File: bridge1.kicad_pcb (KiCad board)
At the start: 2 copper layers, 64 x 50 mm, 14 parts, among them J1 Conn_01x04, U1 pico

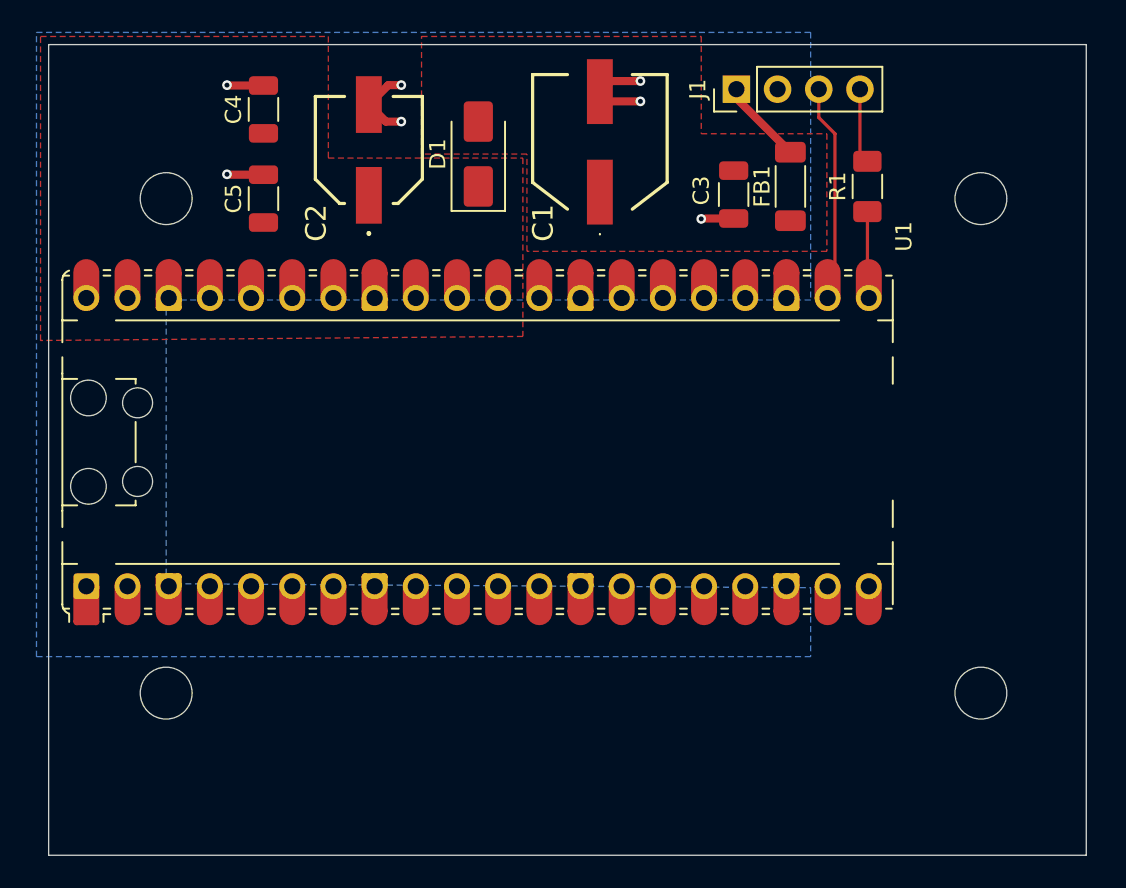
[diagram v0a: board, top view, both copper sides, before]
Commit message: Updated schematic and PCB files to change R1 to 0603 package, J1 to green screw terminal block.
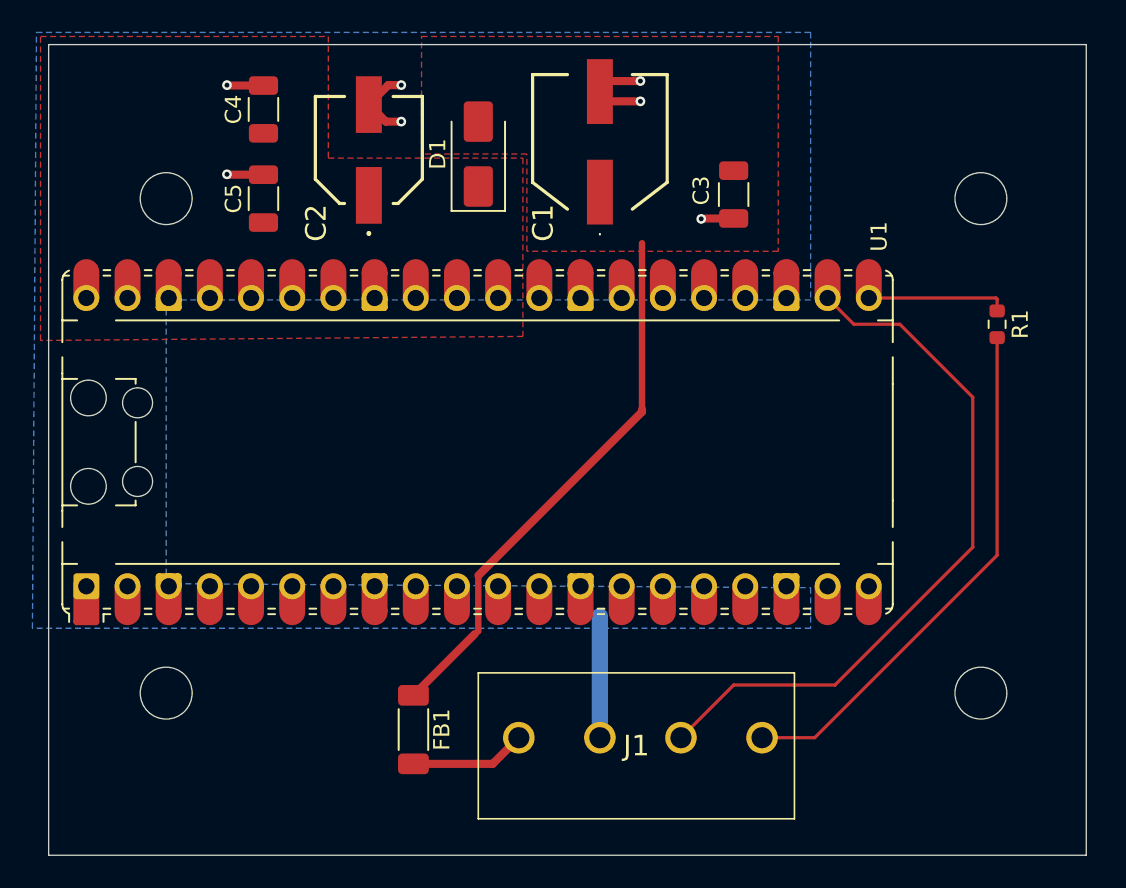
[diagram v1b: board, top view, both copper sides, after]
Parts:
- J1: value Conn_01x04 -> 1935187; footprint Connector_PinHeader_2.54mm:PinHeader_1x04_P2.54mm_Vertical -> Wayne:1935187
- R1: footprint Resistor_SMD:R_1206_3216Metric_Pad1.30x1.75mm_HandSolder -> Resistor_SMD:R_0603_1608Metric
- U1: footprint Wayne:RaspberryPi_Pico_Common_Unspecified -> Module:RaspberryPi_Pico_Common_Unspecified
- moved J1 42.2 mm to (205.0, 88.5), turned to 0 degrees
- moved FB1 40.8 mm to (198.5, 88.0), turned to -90 degrees
- moved R1 11.7 mm to (234.5, 63.0), turned to -90 degrees
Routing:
- net Net-(D1-A): track 0.00 -> 33.4 mm
- net /uart_rx: track 12.7 -> 44.3 mm
- net /uart_tx: track 4.64 -> 32.6 mm
- net GND: track 17.0 -> 24.5 mm
- net Net-(U1-GP16): track 4.57 -> 8.79 mm
- net Net-(FB1-Pad2): track 5.27 -> 7.17 mm

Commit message: Updated PCB file to optimize layout a bit, add silkscreen text.
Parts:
- moved R1 3.29 mm to (231.6, 61.4), turned to 0 degrees
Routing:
- net Net-(U1-GP16): track 8.79 -> 4.34 mm
- net /uart_tx: track 32.6 -> 35.9 mm
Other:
- board size 64 x 50 mm -> 64 x 49.8 mm
- board text added: "+5V GND rx tx"
- board text added: "Bridge1 V1.0"
- board text added: "Gingernut Labs 2026"
- board text added: "UART to WiFi"
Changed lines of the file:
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@@
 	(footprint "Resistor_SMD:R_0603_1608Metric"
 		(layer "F.Cu")
-		(at 234.5 63 -90)
+		(at 231.625 61.4)
 		(descr "Resistor SMD 0603 (1608 Metric), square (rectangular) end terminal, IPC-7351 nominal, (Body size source: IPC-SM-782 page 72, https://www.pcb-3d.com/wordpress/wp-content/uploads/ipc-sm-782a_amendment_1_and_2.pdf), generated with kicad-footprint-generator")
 		(tags "resistor")
 		(property "Reference" "R1"
-			(at 0 -1.43 270)
+			(at 0 -1.43 0)
 			(layer "F.SilkS")
 			(effects
@@
 		)
 		(property "Value" "150"
-			(at 0 1.43 270)
+			(at 0 1.43 0)
 			(layer "F.Fab")
 			(effects
@@
 		)
 		(property "Datasheet" "~"
-			(at 0 0 270)
+			(at 0 0 0)
 			(layer "F.Fab")
 			(hide yes)
@@
 		)
 		(property "Description" "Resistor"
-			(at 0 0 270)
+			(at 0 0 0)
 			(layer "F.Fab")
 			(hide yes)
@@
 			)
 		)
+		(property "LCSC" "C22808"
+			(at 0 0 90)
+			(layer "F.SilkS")
+			(hide yes)
+			(effects
+				(font
+					(size 1.27 1.27)
+					(thickness 0.15)
+				)
+			)
+		)
 		(property ki_fp_filters "R_*")
 		(sheetname "/")
@@
 		(attr smd)
 		(fp_line
-			(start -0.237258 0.5225)
-			(end 0.237258 0.5225)
+			(start -0.237258 -0.5225)
+			(end 0.237258 -0.5225)
 			(stroke
 				(width 0.12)
@@
 		)
 		(fp_line
-			(start -0.237258 -0.5225)
-			(end 0.237258 -0.5225)
+			(start -0.237258 0.5225)
+			(end 0.237258 0.5225)
 			(stroke
 				(width 0.12)
@@
 		)
 		(fp_text user "${REFERENCE}"
-			(at 0 0 270)
+			(at 0 0 0)
 			(layer "F.Fab")
 			(effects
@@
 		)
 		(pad "1" smd roundrect
-			(at -0.825 0 270)
+			(at -0.825 0)
 			(size 0.8 0.95)
 			(layers "F.Cu" "F.Mask" "F.Paste")
@@
 		)
 		(pad "2" smd roundrect
-			(at 0.825 0 270)
+			(at 0.825 0)
 			(size 0.8 0.95)
 			(layers "F.Cu" "F.Mask" "F.Paste")
@@
 		(tags "Connector")
 		(property "Reference" "J1"
-			(at 7.25 0.5 0)
+			(at -3.9 -4.1 0)
 			(layer "F.SilkS")
 			(effects
@@
 	)
 	(gr_rect
-		(start 176 45.75)
-		(end 240 95.75)
+		(start 176.4 45.6)
+		(end 240.4 95.4)
 		(stroke
 			(width 0.05)
@@
 		(layer "Edge.Cuts")
 	)
+	(gr_text "UART to WiFi"
+		(at 221.1 52.3 0)
+		(layer "F.SilkS")
+		(effects
+			(font
+				(size 1.2 1.5)
+				(thickness 0.2)
+				(bold yes)
+			)
+			(justify left bottom)
+		)
+	)
+	(gr_text "+5V   GND    rx    tx"
+		(at 203.2 83.8 0)
+		(layer "F.SilkS")
+		(effects
+			(font
+				(size 1 1)
+				(thickness 0.1)
+			)
+			(justify left bottom)
+		)
+	)
+	(gr_text "Gingernut Labs\n2026"
+		(at 179.5 92.5 0)
+		(layer "F.SilkS")
+		(effects
+			(font
+				(size 1.2 1.2)
+				(thickness 0.15)
+			)
+			(justify left bottom)
+		)
+	)
+	(gr_text "Bridge1 V1.0"
+		(at 221 49.9 0)
+		(layer "F.SilkS")
+		(effects
+			(font
+				(size 1.5 1.5)
+				(thickness 0.2)
+			)
+			(justify left bottom)
+		)
+	)
 	(segment
 		(start 196.8 50.5)
@@
 	)
 	(segment
+		(start 202.44375 81.94375)
+		(end 202.5 81.94375)
+		(width 0.5)
+		(layer "F.Cu")
+		(net 2)
+	)
+	(segment
 		(start 202.5 78.5)
 		(end 212.6 68.4)
@@
 	(segment
 		(start 198.5 85.8875)
-		(end 202.28591 82.10159)
+		(end 202.44375 81.94375)
 		(width 0.5)
 		(layer "F.Cu")
@@
 	)
 	(segment
-		(start 234.5 77.25)
-		(end 234.5 63.825)
+		(start 220 88.5)
+		(end 223.25 88.5)
 		(width 0.2)
 		(layer "F.Cu")
@@
 	)
 	(segment
-		(start 220 88.5)
-		(end 223.25 88.5)
+		(start 223.25 88.5)
+		(end 234.5 77.25)
 		(width 0.2)
 		(layer "F.Cu")
@@
 	)
 	(segment
-		(start 223.25 88.5)
+		(start 234.5 63.5)
 		(end 234.5 77.25)
 		(width 0.2)
@@
 	)
 	(segment
+		(start 232.45 61.45)
+		(end 234.5 63.5)
+		(width 0.2)
+		(layer "F.Cu")
+		(net 4)
+	)
+	(segment
+		(start 232.45 61.4)
+		(end 232.45 61.45)
+		(width 0.2)
+		(layer "F.Cu")
+		(net 4)
+	)
+	(segment
 		(start 224.5 85.25)
 		(end 218.25 85.25)
@@
 	)
 	(segment
-		(start 234.5 61.45)
-		(end 234.5 62.175)
+		(start 230.780324 61.380324)
+		(end 230.8 61.4)
 		(width 0.2)
 		(layer "F.Cu")
@@
 	(segment
 		(start 226.58491 61.380324)
-		(end 234.430324 61.380324)
-		(width 0.2)
-		(layer "F.Cu")
-		(net 6)
-	)
-	(segment
-		(start 234.430324 61.380324)
-		(end 234.5 61.45)
+		(end 230.780324 61.380324)
 		(width 0.2)
 		(layer "F.Cu")

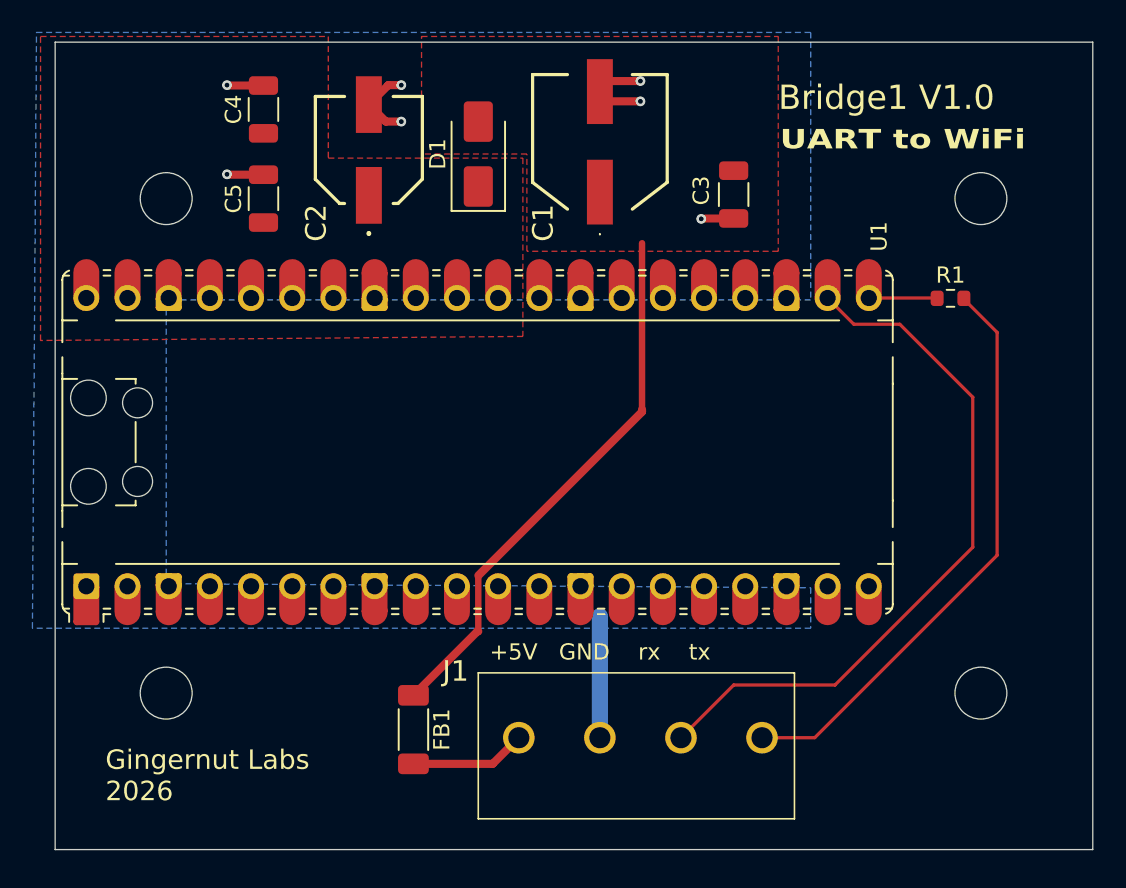
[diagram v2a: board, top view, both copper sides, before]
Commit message: Updated PCB file to properly place mounting holes.
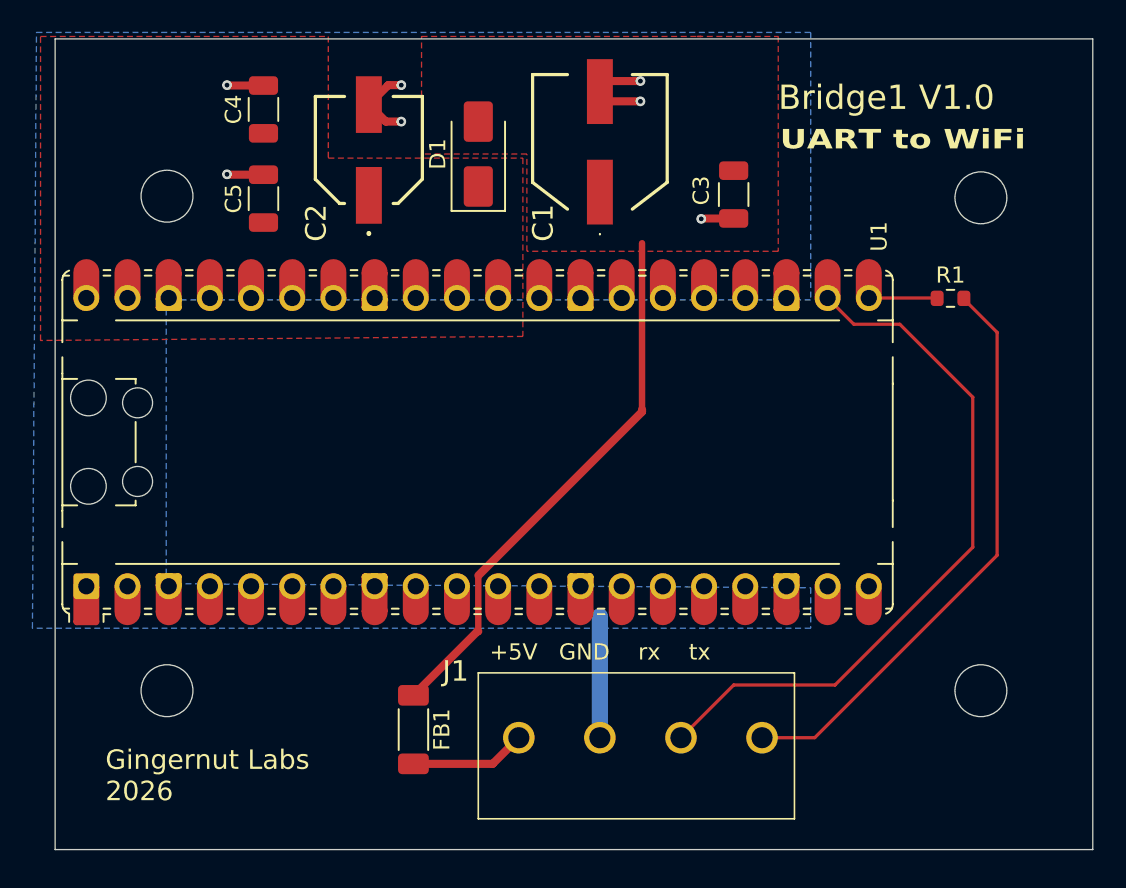
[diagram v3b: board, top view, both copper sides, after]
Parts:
- removed the REF** at (183.2, 55.2)
- removed the REF** at (233.5, 55.2)
- removed the REF** at (233.5, 85.8)
- removed the REF** at (183.2, 85.8)
- added REF**: MountingHole_3.2mm_M3, MountingHole:MountingHole_3.2mm_M3, F.Cu at (183.3, 55.1)
- added REF**: MountingHole_3.2mm_M3, MountingHole:MountingHole_3.2mm_M3, F.Cu at (233.5, 85.6)
- added REF**: MountingHole_3.2mm_M3, MountingHole:MountingHole_3.2mm_M3, F.Cu at (183.3, 85.6)
- added REF**: MountingHole_3.2mm_M3, MountingHole:MountingHole_3.2mm_M3, F.Cu at (233.5, 55.2)
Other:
- board size 64 x 49.8 mm -> 64 x 50 mm
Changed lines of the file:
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@@
 		(allow_soldermask_bridges_in_footprints no)
 		(tenting front back)
+		(aux_axis_origin 176.4 95.4)
+		(grid_origin 176.4 95.4)
 		(pcbplotparams
 			(layerselection 0x00000000_00000000_55555555_5755f5ff)
@@
 	(footprint "MountingHole:MountingHole_3.2mm_M3"
 		(layer "F.Cu")
-		(at 183.25 55.25)
+		(at 183.3 55.1)
 		(descr "Mounting Hole 3.2mm, M3, no annular, generated by kicad-footprint-generator mountinghole.py")
 		(tags "mountinghole M3")
@@
 	(footprint "MountingHole:MountingHole_3.2mm_M3"
 		(layer "F.Cu")
-		(at 233.5 55.25)
+		(at 233.5 85.6)
 		(descr "Mounting Hole 3.2mm, M3, no annular, generated by kicad-footprint-generator mountinghole.py")
 		(tags "mountinghole M3")
@@
 		)
 	)
-	(footprint "MountingHole:MountingHole_3.2mm_M3"
-		(layer "F.Cu")
-		(at 233.5 85.75)
-		(descr "Mounting Hole 3.2mm, M3, no annular, generated by kicad-footprint-generator mountinghole.py")
-		(tags "mountinghole M3")
-		(property "Reference" "REF**"
-			(at 0 -4.15 0)
-			(layer "F.SilkS")
-			(hide yes)
-			(effects
-				(font
-					(size 1 1)
-					(thickness 0.15)
-				)
-			)
-		)
-		(property "Value" "MountingHole_3.2mm_M3"
-			(at 0 4.15 0)
-			(layer "F.Fab")
-			(effects
-				(font
-					(size 1 1)
-					(thickness 0.15)
-				)
-			)
-		)
-		(property "Datasheet" ""
-			(at 0 0 0)
-			(layer "F.Fab")
-			(hide yes)
-			(effects
-				(font
-					(size 1.27 1.27)
-					(thickness 0.15)
-				)
-			)
-		)
-		(property "Description" ""
-			(at 0 0 0)
-			(layer "F.Fab")
-			(hide yes)
-			(effects
-				(font
-					(size 1.27 1.27)
-					(thickness 0.15)
-				)
-			)
-		)
-		(attr exclude_from_pos_files exclude_from_bom)
-		(fp_circle
-			(center 0 0)
-			(end 3.2 0)
-			(stroke
-				(width 0.15)
-				(type solid)
-			)
-			(fill no)
-			(layer "Cmts.User")
-		)
-		(fp_circle
-			(center 0 0)
-			(end 3.45 0)
-			(stroke
-				(width 0.05)
-				(type solid)
-			)
-			(fill no)
-			(layer "F.CrtYd")
-		)
-		(fp_text user "${REFERENCE}"
-			(at 0 0 0)
-			(layer "F.Fab")
-			(effects
-				(font
-					(size 1 1)
-					(thickness 0.15)
-				)
-			)
-		)
-		(pad "" np_thru_hole circle
-			(at 0 0)
-			(size 3.2 3.2)
-			(drill 3.2)
-			(layers "*.Cu" "*.Mask")
-		)
-		(embedded_fonts no)
-	)
 	(footprint "Resistor_SMD:R_0603_1608Metric"
 		(layer "F.Cu")
@@
 	(footprint "MountingHole:MountingHole_3.2mm_M3"
 		(layer "F.Cu")
-		(at 183.25 85.75)
+		(at 183.3 85.6)
 		(descr "Mounting Hole 3.2mm, M3, no annular, generated by kicad-footprint-generator mountinghole.py")
 		(tags "mountinghole M3")
@@
 		)
 	)
+	(footprint "MountingHole:MountingHole_3.2mm_M3"
+		(layer "F.Cu")
+		(at 233.5 55.2)
+		(descr "Mounting Hole 3.2mm, M3, no annular, generated by kicad-footprint-generator mountinghole.py")
+		(tags "mountinghole M3")
+		(property "Reference" "REF**"
+			(at 0 -4.15 0)
+			(layer "F.SilkS")
+			(hide yes)
+			(effects
+				(font
+					(size 1 1)
+					(thickness 0.15)
+				)
+			)
+		)
+		(property "Value" "MountingHole_3.2mm_M3"
+			(at 0 4.15 0)
+			(layer "F.Fab")
+			(effects
+				(font
+					(size 1 1)
+					(thickness 0.15)
+				)
+			)
+		)
+		(property "Datasheet" ""
+			(at 0 0 0)
+			(layer "F.Fab")
+			(hide yes)
+			(effects
+				(font
+					(size 1.27 1.27)
+					(thickness 0.15)
+				)
+			)
+		)
+		(property "Description" ""
+			(at 0 0 0)
+			(layer "F.Fab")
+			(hide yes)
+			(effects
+				(font
+					(size 1.27 1.27)
+					(thickness 0.15)
+				)
+			)
+		)
+		(attr exclude_from_pos_files exclude_from_bom)
+		(fp_circle
+			(center 0 0)
+			(end 3.2 0)
+			(stroke
+				(width 0.15)
+				(type solid)
+			)
+			(fill no)
+			(layer "Cmts.User")
+		)
+		(fp_circle
+			(center 0 0)
+			(end 3.45 0)
+			(stroke
+				(width 0.05)
+				(type solid)
+			)
+			(fill no)
+			(layer "F.CrtYd")
+		)
+		(fp_text user "${REFERENCE}"
+			(at 0 0 0)
+			(layer "F.Fab")
+			(effects
+				(font
+					(size 1 1)
+					(thickness 0.15)
+				)
+			)
+		)
+		(pad "" np_thru_hole circle
+			(at 0 0)
+			(size 3.2 3.2)
+			(drill 3.2)
+			(layers "*.Cu" "*.Mask")
+		)
+		(embedded_fonts no)
+	)
 	(gr_rect
-		(start 176.4 45.6)
+		(start 176.4 45.4)
 		(end 240.4 95.4)
 		(stroke

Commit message: Updated PCB file to widen the UART tracks to 0.4mm from 0.2mm
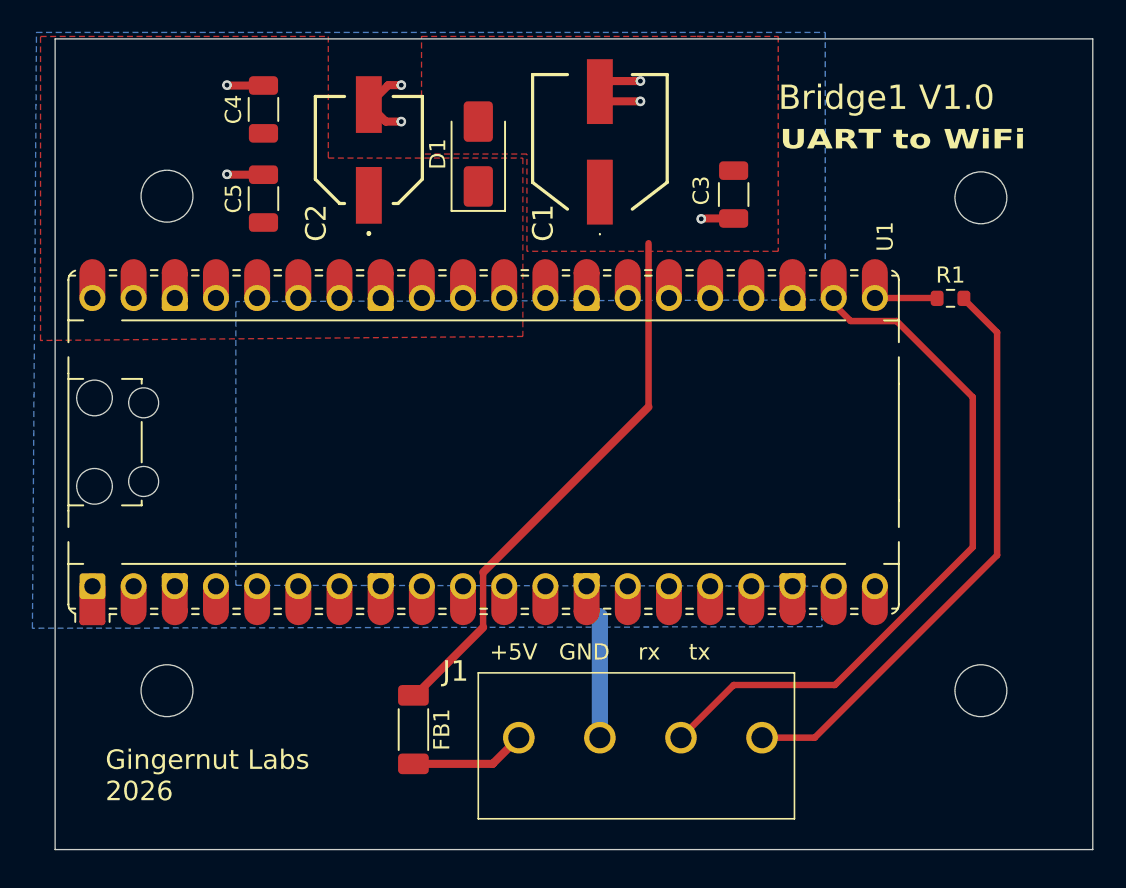
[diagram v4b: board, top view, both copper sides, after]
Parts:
- moved U1 0.38 mm to (202.8, 70.3)
